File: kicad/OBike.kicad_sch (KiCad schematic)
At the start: 62 parts, among them J1 62684-402100ALF, J2 Micro_SD_Card_Det1, J3 Conn_01x02, J5 U.FL-R-SMT-1_10_, J6 Conn_01x02, SW1 5_position_tactile, U1 DPS368XTSA1, U10 MAX40200AUK, U2 DS3231M, U3 MCP23017_SO, U4 74HC14, U5 Seeed Studio XIAO SAMD21, U6 MAX40200AUK, U7 LC76G, U8 MAX40200AUK, U9 W25N01GVZEIG_TR

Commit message: Purchased PCBs
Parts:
- added C13: 0.1uF, Capacitor_SMD:C_0805_2012Metric, symbol Device:C
- added C14: 1.0uF, Capacitor_SMD:C_0805_2012Metric, symbol Device:C
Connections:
- net AUX_3V3: now also C13.1, C14.1
- net GND: now also C13.2, C14.2
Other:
- moved on the sheet: U9

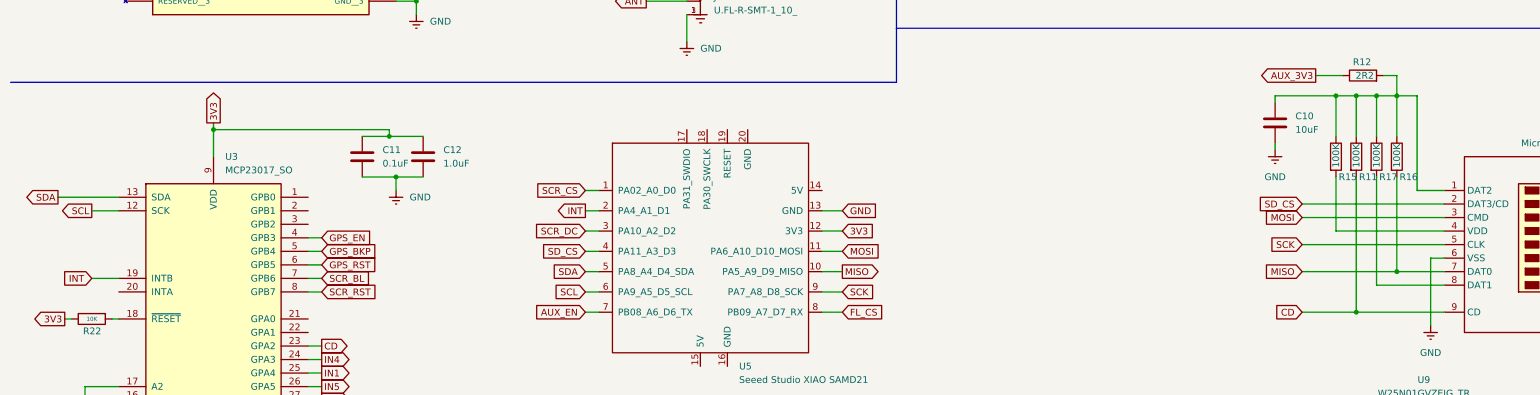
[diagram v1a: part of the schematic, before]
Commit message: migrate to platform IO
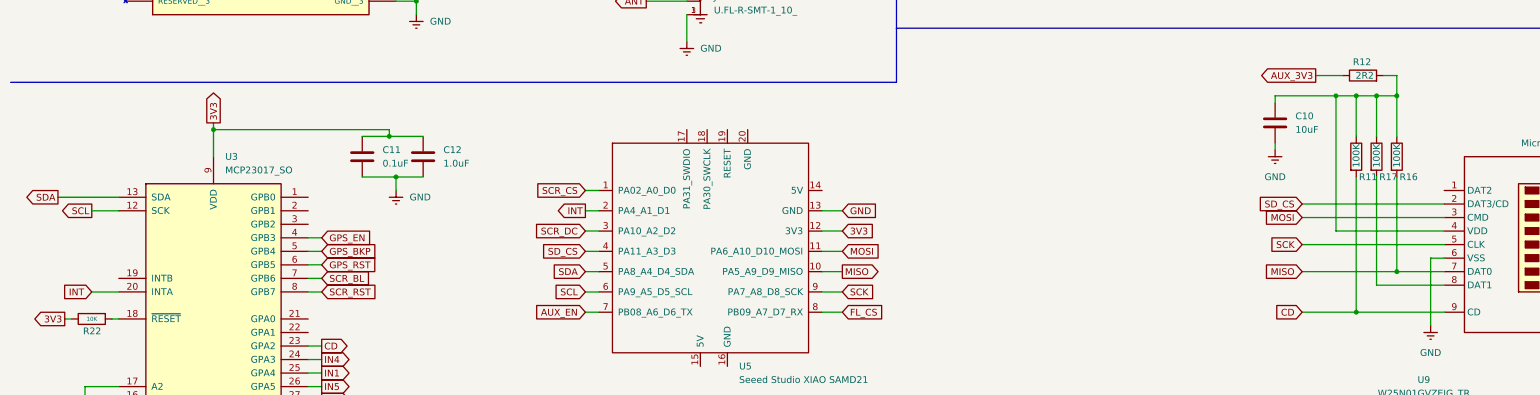
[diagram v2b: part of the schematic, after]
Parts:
- removed R15: 100K, Resistor_SMD:R_0603_1608Metric, symbol Device:R
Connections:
- net INT: now also U3.20 (INTA); no longer U3.19 (INTB)
- net at C10.1, R11.1, R12.2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: now also J2.4 (VDD); no longer J2.1 (DAT2)
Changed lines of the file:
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@@
 	(wire
 		(pts
-			(xy 261.62 163.83) (xy 261.62 173.99)
+			(xy 261.62 148.59) (xy 261.62 173.99)
 		)
 		(stroke
@@
 	(wire
 		(pts
-			(xy 281.94 166.37) (xy 276.86 166.37)
-		)
-		(stroke
-			(width 0)
-			(type default)
-		)
-	)
-	(wire
-		(pts
-			(xy 261.62 148.59) (xy 261.62 156.21)
-		)
-		(stroke
-			(width 0)
-			(type default)
-		)
-	)
-	(wire
-		(pts
 			(xy 116.84 107.95) (xy 121.92 107.95)
 		)
@@
 	(wire
 		(pts
-			(xy 27.94 182.88) (xy 33.02 182.88)
-		)
-		(stroke
-			(width 0)
-			(type default)
-		)
-	)
-	(wire
-		(pts
 			(xy 252.73 34.29) (xy 254 34.29)
 		)
@@
 	(wire
 		(pts
-			(xy 293.37 116.84) (xy 297.18 116.84)
+			(xy 27.94 185.42) (xy 33.02 185.42)
 		)
 		(stroke
@@
 	(wire
 		(pts
-			(xy 120.65 181.61) (xy 123.19 181.61)
+			(xy 293.37 116.84) (xy 297.18 116.84)
 		)
 		(stroke
@@
 	(wire
 		(pts
-			(xy 302.26 219.71) (xy 302.26 218.44)
+			(xy 120.65 181.61) (xy 123.19 181.61)
 		)
 		(stroke
@@
 	(wire
 		(pts
-			(xy 273.05 148.59) (xy 276.86 148.59)
+			(xy 302.26 219.71) (xy 302.26 218.44)
 		)
 		(stroke
@@
 	(wire
 		(pts
-			(xy 276.86 148.59) (xy 276.86 166.37)
-		)
-		(stroke
-			(width 0)
-			(type default)
-		)
-	)
-	(wire
-		(pts
 			(xy 50.8 153.67) (xy 50.8 154.94)
 		)
@@
 	(global_label "INT"
 		(shape input)
-		(at 27.94 182.88 180)
+		(at 27.94 185.42 180)
 		(fields_autoplaced yes)
 		(effects
@@
 		)
 		(property "Intersheetrefs" "${INTERSHEET_REFS}"
-			(at 22.0519 182.88 0)
+			(at 22.0519 185.42 0)
 			(effects
 				(font
@@
 					(unit 1)
 				)
-			)
-		)
-	)
-	(symbol
-		(lib_id "Device:R")
-		(at 261.62 160.02 0)
-		(unit 1)
-		(exclude_from_sim no)
-		(in_bom yes)
-		(on_board yes)
-		(dnp no)
-		(property "Reference" "R15"
-			(at 262.128 163.83 0)
-			(effects
-				(font
-					(size 1.27 1.27)
-				)
-				(justify left)
-			)
-		)
-		(property "Value" "100K"
-			(at 261.62 162.052 90)
-			(effects
-				(font
-					(size 1.27 1.27)
-				)
-				(justify left)
-			)
-		)
-		(property "Footprint" "Resistor_SMD:R_0603_1608Metric"
-			(at 259.842 160.02 90)
-			(effects
-				(font
-					(size 1.27 1.27)
-				)
-				(hide yes)
-			)
-		)
-		(property "Datasheet" "~"
-			(at 261.62 160.02 0)
-			(effects
-				(font
-					(size 1.27 1.27)
-				)
-				(hide yes)
-			)
-		)
-		(property "Description" "Resistor"
-			(at 261.62 160.02 0)
-			(effects
-				(font
-					(size 1.27 1.27)
-				)
-				(hide yes)
-			)
-		)
-		(property "MANUFACTURER" ""
-			(at 261.62 160.02 0)
-			(effects
-				(font
-					(size 1.27 1.27)
-				)
-				(hide yes)
-			)
-		)
-		(property "Digikiey PN" "RMCF0603FT100KCT-ND"
-			(at 261.62 160.02 0)
-			(effects
-				(font
-					(size 1.27 1.27)
-				)
-				(hide yes)
-			)
-		)
-		(pin "1"
-		)
-		(pin "2"
-		)
-		(instances
-			(project "OBike"
-				(path "/b6c91502-91b9-44d0-9569-7774925b5f71"
-					(reference "R15")
-					(unit 1)
-				)

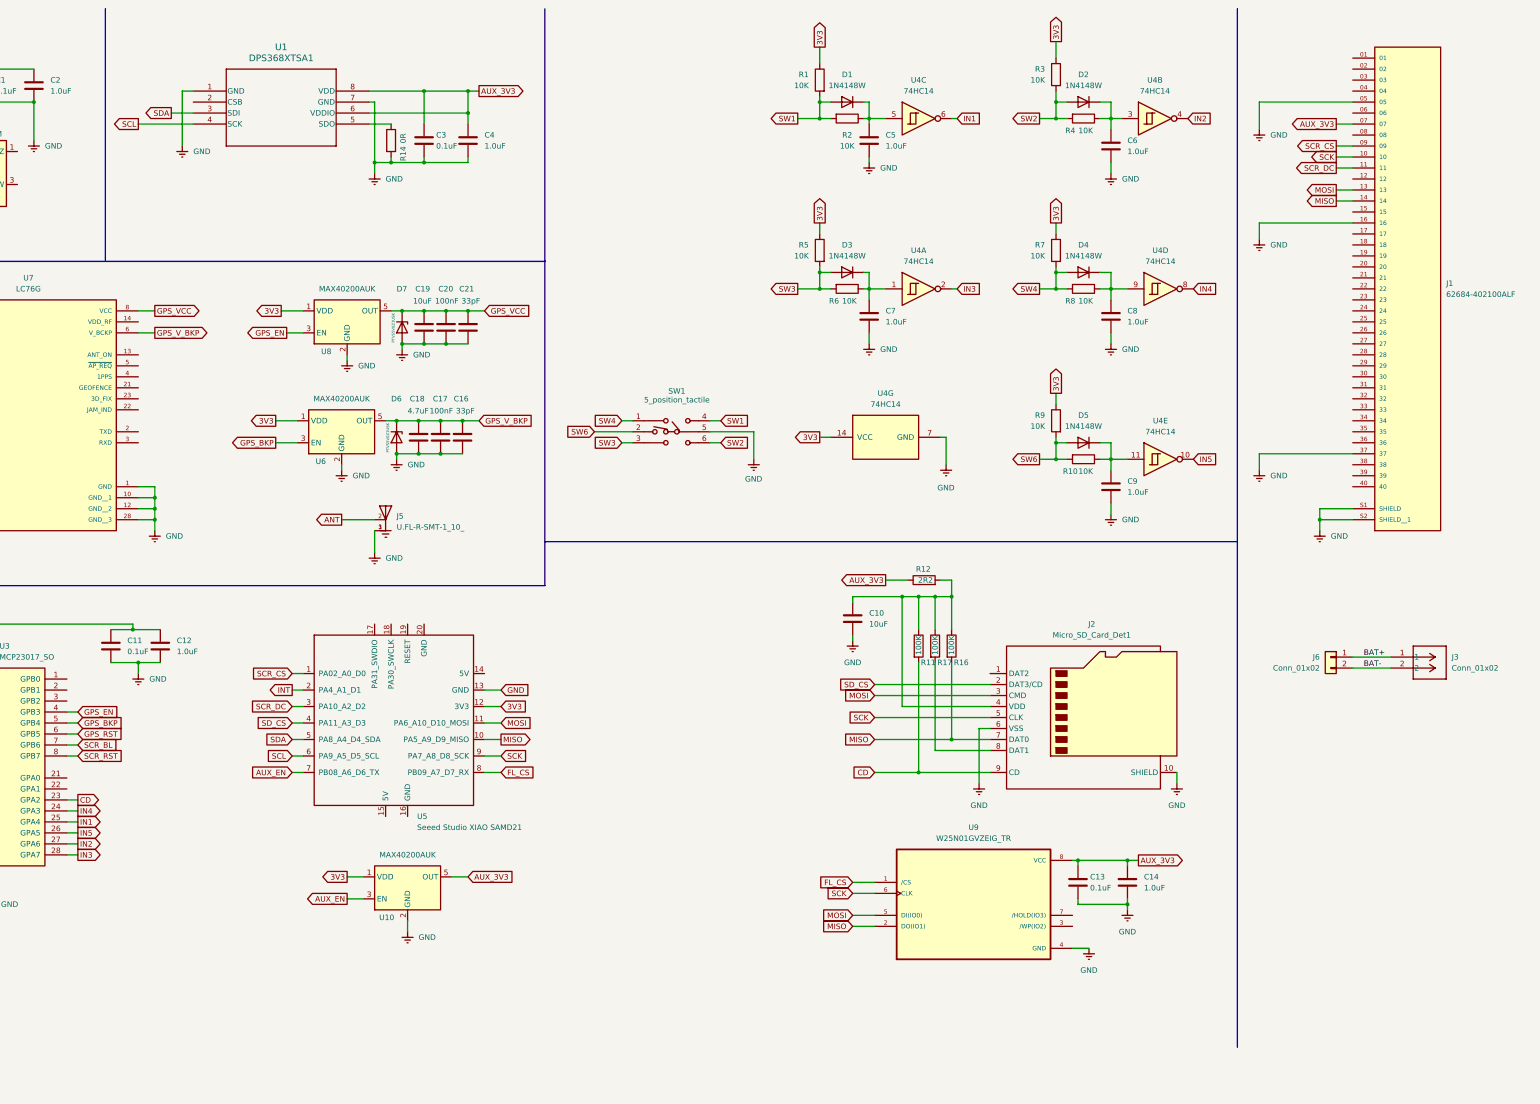
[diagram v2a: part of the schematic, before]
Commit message: LCD interface
fixed mistakes in FPC connector nets
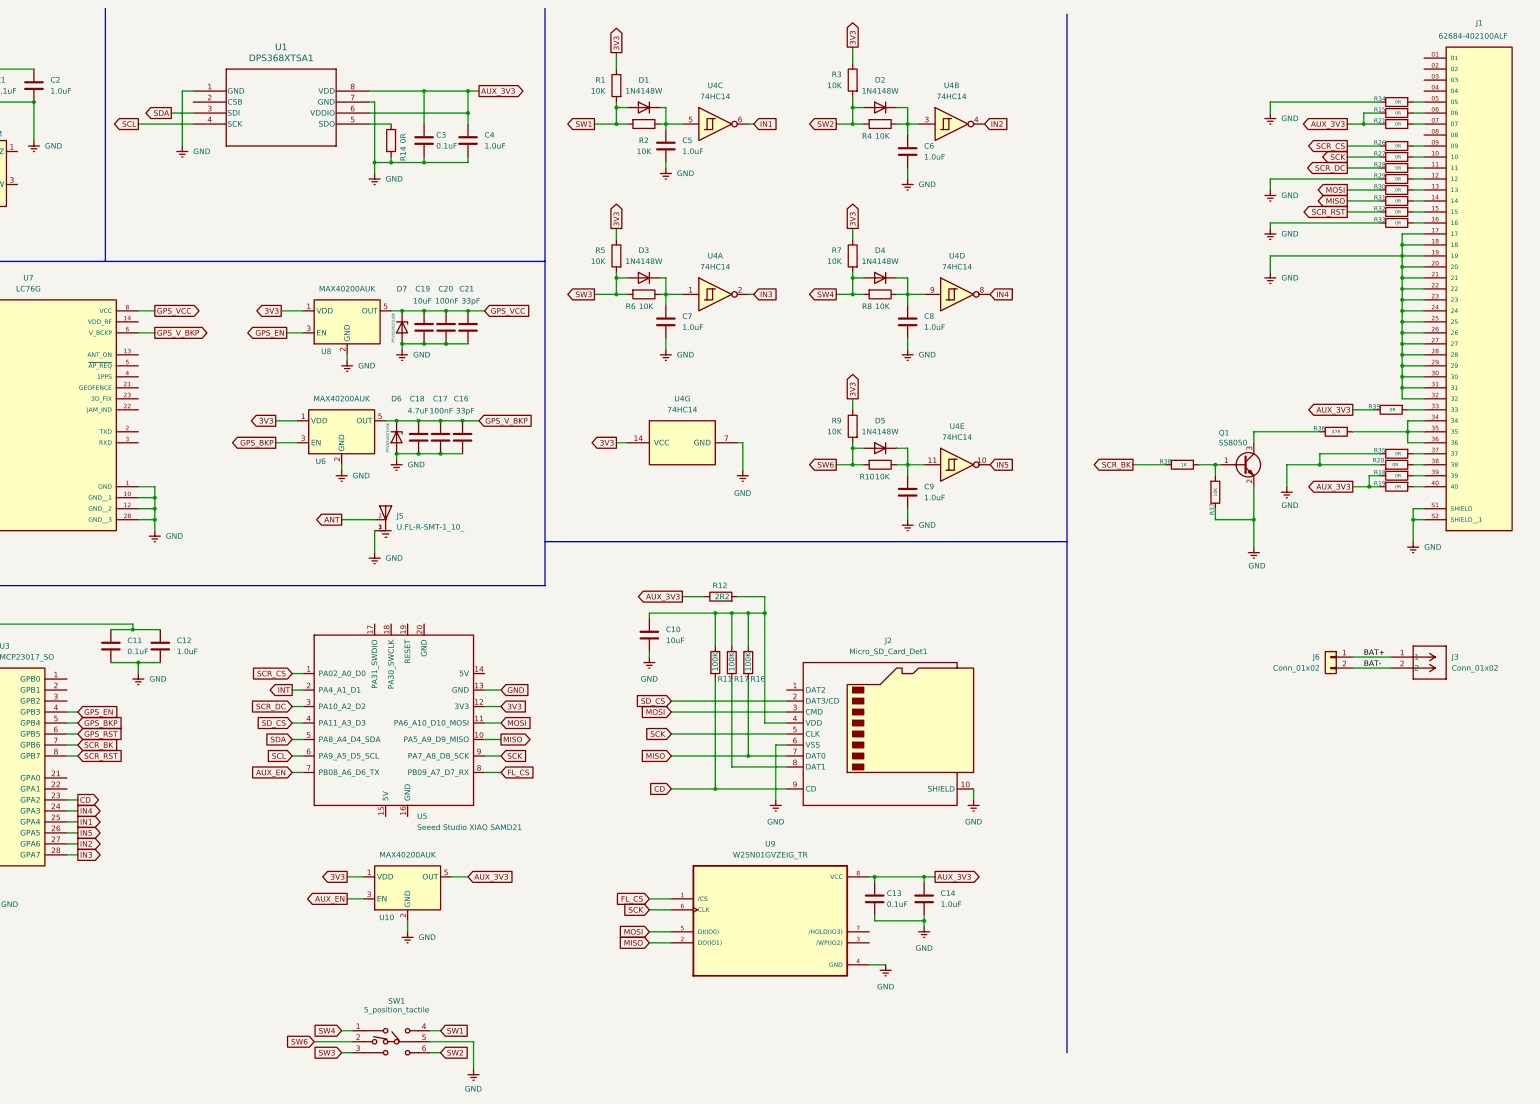
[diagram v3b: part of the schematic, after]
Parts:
- added Q1: SS8050, Package_TO_SOT_SMD:SOT-23, symbol Transistor_BJT:SS8050
- added R15, R18, R19, R20, R21, R26, R27, R28, R29, R30, R31, R32, R33, R34, R35, R39: 0R, Resistor_SMD:R_0402_1005Metric, symbol Device:R
- added R36: 47R, Resistor_SMD:R_0603_1608Metric, symbol Device:R
- added R37: 10K, Resistor_SMD:R_0603_1608Metric, symbol Device:R
- added R38: 1K, Resistor_SMD:R_0603_1608Metric, symbol Device:R
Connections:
- net AUX_3V3: now also R15.1, R18.1, R19.1, R21.1, R39.1; no longer J1.07
- net GND: now also J1.17, J1.18, J1.19, J1.20, J1.21, J1.22, J1.23, J1.24, J1.25, J1.26, J1.27, J1.28, J1.29, J1.30, J1.31, J1.32, Q1.2 (E), R20.2, R29.1, R33.1, R34.1, R35.1, R37.1; no longer J1.05, J1.16, J1.37
- net MISO: now also R31.1; no longer J1.14
- net MOSI: now also R30.1; no longer J1.13
- net SCK: now also R27.1; no longer J1.10
- net SCR_CS: now also R26.1; no longer J1.09
- net SCR_DC: now also R28.1; no longer J1.11
- net SCR_RST: now also R32.1
- net at J1.06: now also R15.2
- net at J1.12: now also R29.2
- net at J1.15: now also R32.2
- net at J1.33: now also R39.2
- net at J1.34: now also J1.35, J1.36, R36.2
- net at J1.38: now also R20.1
- net at J1.39: now also R18.2
- net at J1.40: now also R19.2
- net SCR_BL renamed SCR_BK
- net SCR_BK: now also R38.1
- new net: J1.05, R34.2
- new net: J1.07, R21.2
- new net: J1.09, R26.2
- new net: J1.10, R27.2
- new net: J1.11, R28.2
- new net: J1.13, R30.2
- new net: J1.14, R31.2
- new net: J1.16, R33.2
- new net: J1.37, R35.2
- new net: Q1.3 (C), R36.1
- new net: Q1.1 (B), R37.2, R38.2
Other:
- moved on the sheet: C10, C13, C14, C5, C6, C7, C8, C9, D1, D2, D3, D4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

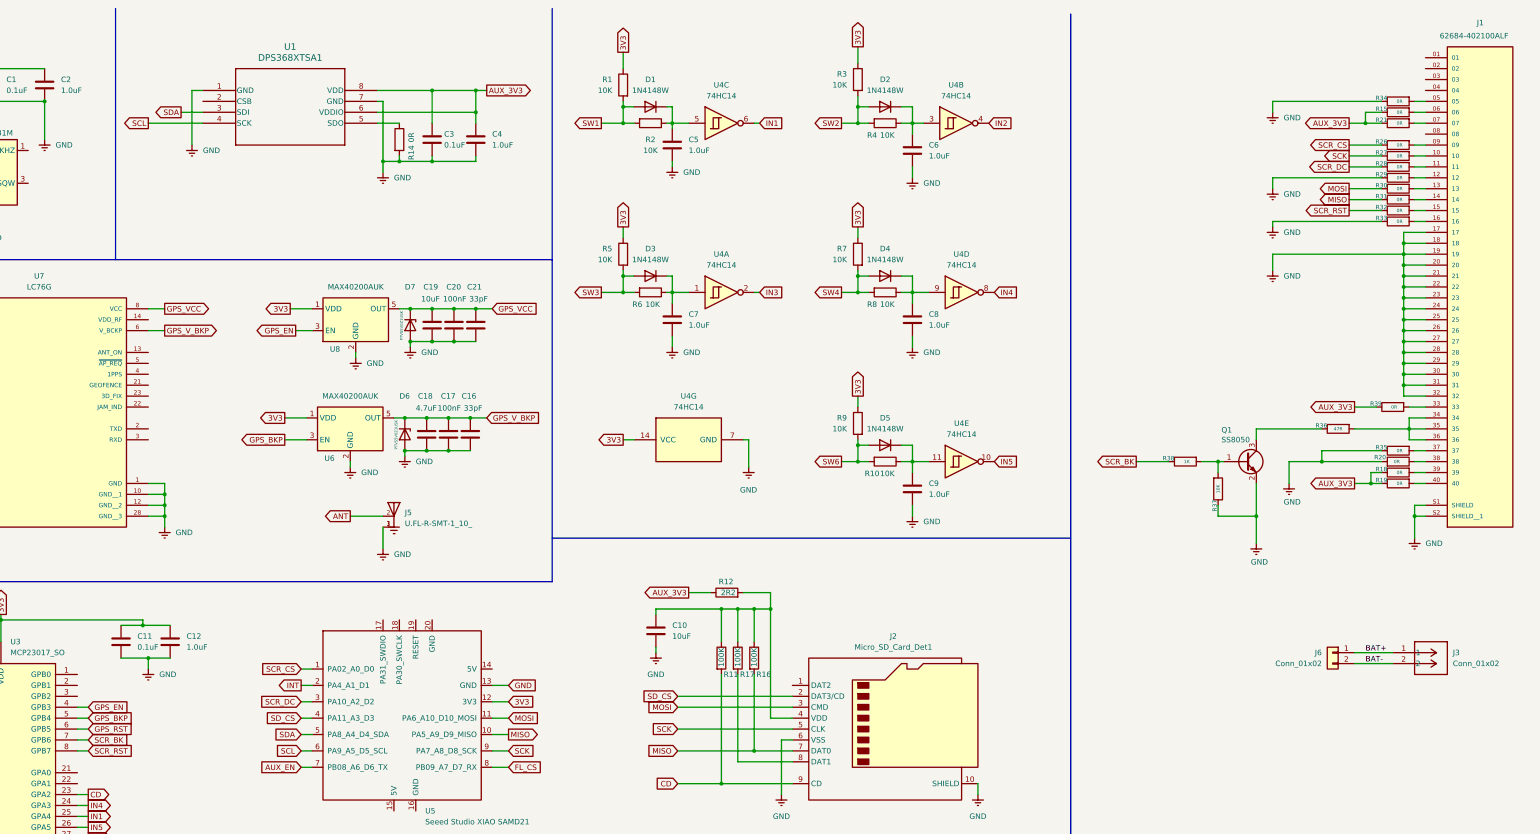
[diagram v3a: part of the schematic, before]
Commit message: screen fpc
- changed fpc to bottom mount pins
- changed fpc footprint and symbol
- updated fpc routing
- added JST connectors for SPI & I2C expansion
- stopped tracking kicad/*.zip
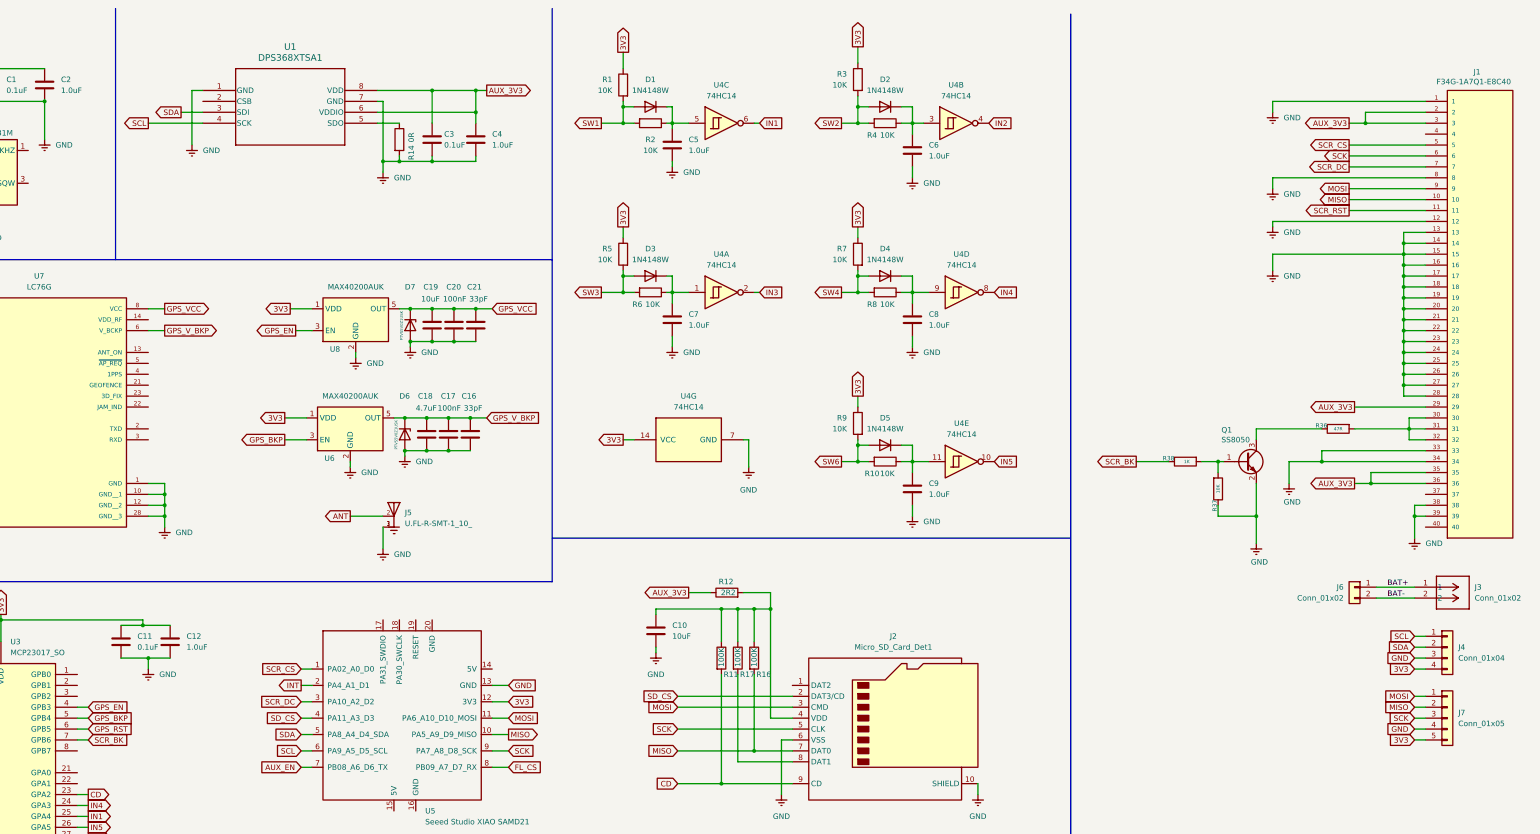
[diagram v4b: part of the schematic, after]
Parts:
- removed J1: 62684-402100ALF, amphenol:AMPHENOL_62684-402100ALF, symbol amphenol:62684-402100ALF
- removed R15, R18, R19, R20, R21, R26, R27, R28, R29, R30, R31, R32, R33, R34, R35, R39: 0R, Resistor_SMD:R_0402_1005Metric, symbol Device:R
- added J1: F34G-1A7Q1-E8C40, amphenol:AMPHENOL_F34G-1A7Q1-E8C40, symbol amphenol_F34G:F34G-1A7Q1-E8C40
- added J4: Conn_01x04, Connector_JST:JST_GH_SM04B-GHS-TB_1x04-1MP_P1.25mm_Horizontal, symbol Connector_Generic:Conn_01x04
- added J7: Conn_01x05, Connector_JST:JST_GH_SM05B-GHS-TB_1x05-1MP_P1.25mm_Horizontal, symbol Connector_Generic:Conn_01x05
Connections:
- net 3V3: now also J4.4 (Pin_4), J7.5 (Pin_5)
- net AUX_3V3: now also J1.2, J1.29, J1.3, J1.35, J1.36
- net GND: now also J1.1, J1.12, J1.13, J1.14, J1.15, J1.16, J1.17, J1.18, J1.19, J1.20, J1.21, J1.22, J1.23, J1.24, J1.25, J1.26, J1.27, J1.28, J1.33, J1.34, J1.38, J1.39, J1.8, J4.3 (Pin_3), J7.4 (Pin_4)
- net MISO: now also J1.10, J7.2 (Pin_2)
- net MOSI: now also J1.9, J7.1 (Pin_1)
- net SCK: now also J1.6, J7.3 (Pin_3)
- net SCL: now also J4.1 (Pin_1)
- net SCR_CS: now also J1.5
- net SCR_DC: now also J1.7
- net SCR_RST: now also J1.11; no longer U3.8 (GPB7)
- net SDA: now also J4.2 (Pin_2)
- net at R36.2: now also J1.30, J1.31, J1.32
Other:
- moved on the sheet: J3, J6

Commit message: pcb update
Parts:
- removed J6: Conn_01x02, symbol Connector_Generic:Conn_01x02
- added LS1: PK-11N40PQ, Mallory:PK-11N40PQ_MAL, symbol Mallory:PK-11N40PQ
- J4: footprint Connector_JST:JST_GH_SM04B-GHS-TB_1x04-1MP_P1.25mm_Horizontal -> Connector_PinHeader_2.54mm:PinHeader_1x04_P2.54mm_Vertical; now not fitted
- J7: footprint Connector_JST:JST_GH_SM05B-GHS-TB_1x05-1MP_P1.25mm_Horizontal -> Connector_PinHeader_2.54mm:PinHeader_1x05_P2.54mm_Vertical; now not fitted
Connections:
- net AUX_3V3: now also J1.33, J1.39, J1.40, J1.6, J1.7; no longer J1.2, J1.29, J1.3, J1.35, J1.36
- net GND: now also J1.29, J1.30, J1.31, J1.32, J1.37, J1.5, LS1.2; no longer J1.1, J1.13, J1.14, J1.15, J1.33, J1.34, J1.39, J1.8
- net INT: now also U5.4 (PA11_A3_D3); no longer U5.2 (PA4_A1_D1)
- net MISO: now also J1.14, J7.1 (Pin_1); no longer J1.10, J7.2 (Pin_2)
- net MOSI: now also J1.13, J7.2 (Pin_2); no longer J1.9, J7.1 (Pin_1)
- net SCK: now also J1.10; no longer J1.6
- net SCL: now also J4.2 (Pin_2); no longer J4.1 (Pin_1)
- net SCR_CS: now also J1.9; no longer J1.5
- net SCR_DC: now also J1.11; no longer J1.7
- net SCR_RST: now also J1.15; no longer J1.11
- net SDA: now also J4.1 (Pin_1); no longer J4.2 (Pin_2)
- net SD_CS: now also U5.2 (PA4_A1_D1); no longer U5.4 (PA11_A3_D3)
- net BUZZ: now reaches U3.3 (GPB2)
- net BUZZ: now also LS1.1
- new net: J1.34, J1.35, J1.36, R36.2
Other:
- moved on the sheet: J1
